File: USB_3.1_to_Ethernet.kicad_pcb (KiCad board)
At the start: 4 copper layers, 76 x 25 mm, 79 parts, among them J1 RJ45_JK0654219, J2 USB3_A, U1 LAN7801_9JX, U2 93LC56B_SN, U3 KSZ9031RNXCC, U4 TLV76733, U5 USBLC6-2P6, U6 TPS7A0212, Y1 25MHz, Y2 25MHz

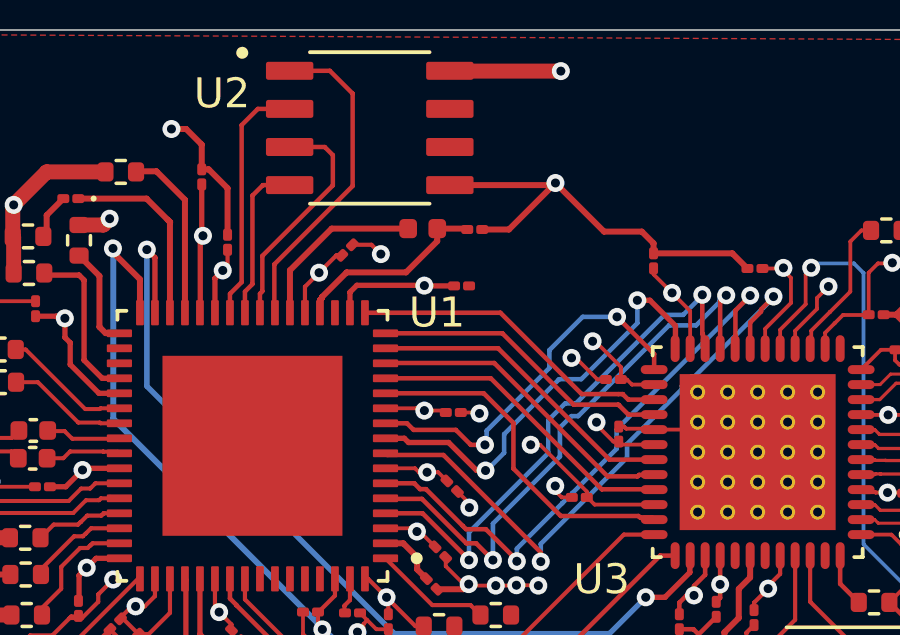
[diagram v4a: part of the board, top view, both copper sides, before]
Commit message: microadjustments  in via connections of  gnd
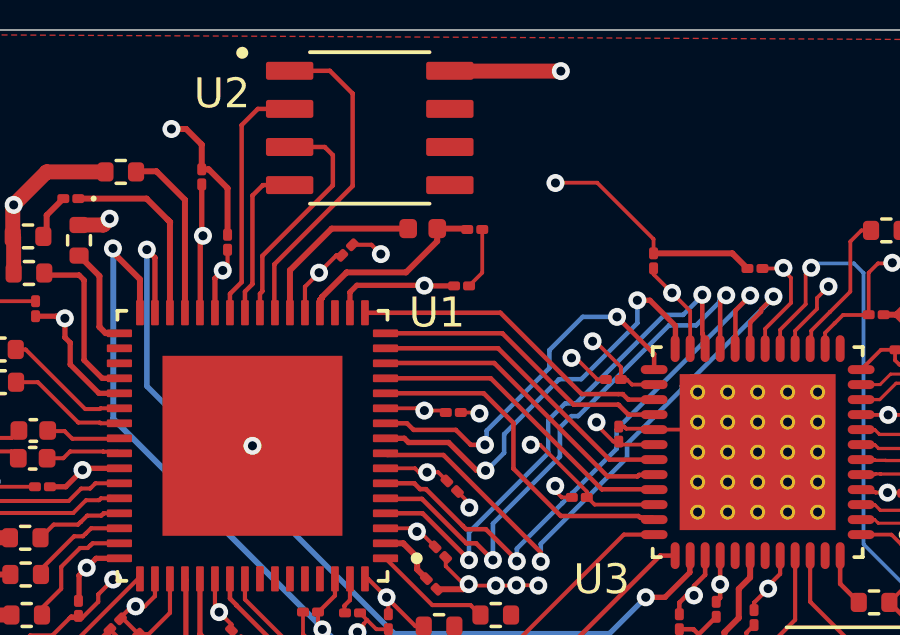
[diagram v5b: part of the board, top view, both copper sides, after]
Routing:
- net GND: track 144.6 -> 140.1 mm, vias 32 -> 33
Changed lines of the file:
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@@
+	)
+	(segment
+		(start 97.67 57.545)
+		(end 97.67 57.07)
+		(width 0.127)
+		(layer "F.Cu")
+		(net "GND")
 	)
 	(segment
@@
 	)
 	(segment
+		(start 94.41 55.19)
+		(end 94.4 55.2)
+		(width 0.127)
+		(layer "F.Cu")
+		(net "GND")
+	)
+	(segment
+		(start 91.96 58.19)
+		(end 91.96 56.75)
+		(width 0.127)
+		(layer "F.Cu")
+		(net "GND")
+	)
+	(segment
 		(start 70.86 72.79)
 		(end 70.52 72.45)
@@
 		(start 76.23 68.25)
 		(end 75.1 68.25)
-		(width 0.2)
-		(layer "F.Cu")
-		(net "GND")
-	)
-	(segment
-		(start 90.88 55.27)
-		(end 94.33 55.27)
 		(width 0.2)
 		(layer "F.Cu")
@@
 	)
 	(segment
+		(start 91.52 58.63)
+		(end 91.96 58.19)
+		(width 0.127)
+		(layer "F.Cu")
+		(net "GND")
+	)
+	(segment
 		(start 83.47 55.373722)
 		(end 83.47 56.925)
-		(width 0.2)
-		(layer "F.Cu")
-		(net "GND")
-	)
-	(segment
-		(start 94.33 55.27)
-		(end 94.4 55.2)
 		(width 0.2)
 		(layer "F.Cu")
@@
 	)
 	(segment
+		(start 97.67 57.07)
+		(end 95.79 55.19)
+		(width 0.127)
+		(layer "F.Cu")
+		(net "GND")
+	)
+	(segment
 		(start 105.26 72.57)
 		(end 106.255 73.565)
@@
 	)
 	(segment
+		(start 95.79 55.19)
+		(end 94.41 55.19)
+		(width 0.127)
+		(layer "F.Cu")
+		(net "GND")
+	)
+	(segment
 		(start 86.396922 70.6427)
 		(end 85.985 70.230778)
@@
 	)
 	(segment
-		(start 97.67 57.21)
-		(end 97.67 57.545)
-		(width 0.2)
-		(layer "F.Cu")
-		(net "GND")
-	)
-	(segment
 		(start 82.61 54.745)
 		(end 82.841278 54.745)
@@
 		(end 97.69 63.42)
 		(width 0.127)
-		(layer "F.Cu")
-		(net "GND")
-	)
-	(segment
-		(start 91.96 56.75)
-		(end 92.85 56.75)
-		(width 0.2)
 		(layer "F.Cu")
 		(net "GND")
@@
 	)
 	(segment
-		(start 96.02 56.82)
-		(end 97.28 56.82)
-		(width 0.2)
-		(layer "F.Cu")
-		(net "GND")
-	)
-	(segment
-		(start 97.28 56.82)
-		(end 97.67 57.21)
-		(width 0.2)
-		(layer "F.Cu")
-		(net "GND")
-	)
-	(segment
 		(start 83.47 73.64)
 		(end 85.25 73.64)
@@
 		(end 94.945001 65.68)
 		(width 0.127)
-		(layer "F.Cu")
-		(net "GND")
-	)
-	(segment
-		(start 94.4 55.2)
-		(end 96.02 56.82)
-		(width 0.2)
 		(layer "F.Cu")
 		(net "GND")
@@
 		(end 96.689658 63.32)
 		(width 0.127)
-		(layer "F.Cu")
-		(net "GND")
-	)
-	(segment
-		(start 92.85 56.75)
-		(end 94.4 55.2)
-		(width 0.2)
 		(layer "F.Cu")
 		(net "GND")
@@
 		(size 0.6)
 		(drill 0.3)
+		(layers "F.Cu" "B.Cu")
+		(net "GND")
+	)
+	(via
+		(at 84.299999 63.96)
+		(size 0.6)
+		(drill 0.3)

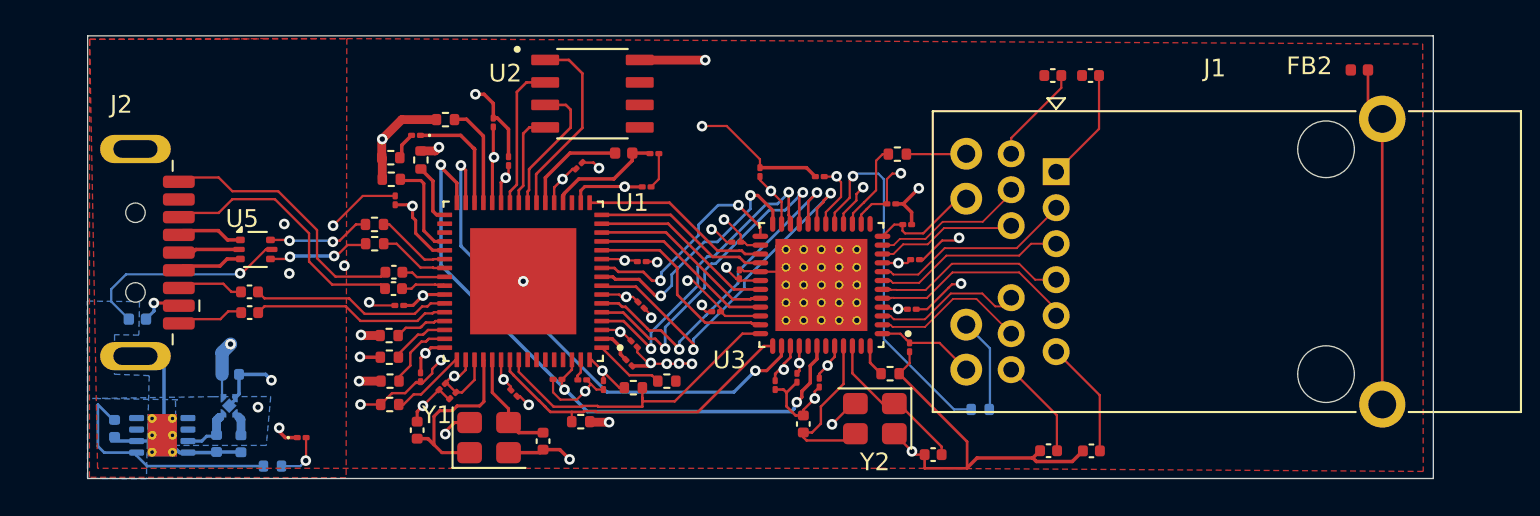
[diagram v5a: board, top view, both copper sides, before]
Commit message: cleaned the DRC errors and step files of ICs included
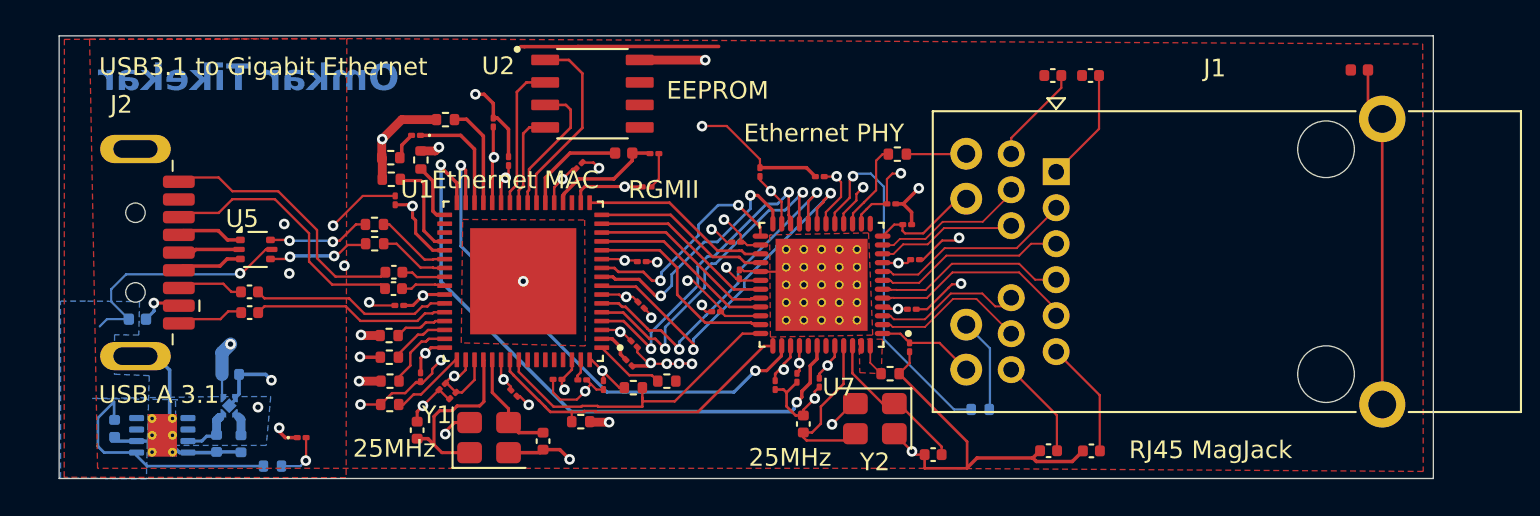
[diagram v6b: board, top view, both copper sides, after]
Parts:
- removed U3: KSZ9031RNXCC, KSZ9031RNX:IC_KSZ9031RNXCC
- added U7: KSZ9031RNXCC, KSZ9031RNXCC:IC_KSZ9031RNXCC, F.Cu at (101.2, 64.2)
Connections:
- C48 pad 1: 3v3_out -> 1v2_core
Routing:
- net GND: track 140.1 -> 151.6 mm
- net 1v2_core: track 125.4 -> 128.4 mm
- net +5V: track 25.6 -> 27.7 mm
- net /~{RESET_N}: track 35.8 -> 36.3 mm
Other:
- board size 76 x 25 mm -> 77.6 x 25 mm
- board text added: "25MHz"
- board text added: "EEPROM"
- board text added: "Ethernet MAC"
- board text added: "Ethernet PHY"
- board text added: "Omkar Tikekar"
- board text added: "RGMII"
- board text added: "RJ45 MagJack"
- board text added: "USB A 3.1"
- board text added: "USB3.1 to Gigabit Ethernet"

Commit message: step file for usb A plug added. Modified edge cuts layer by adding a slot for usb connector'
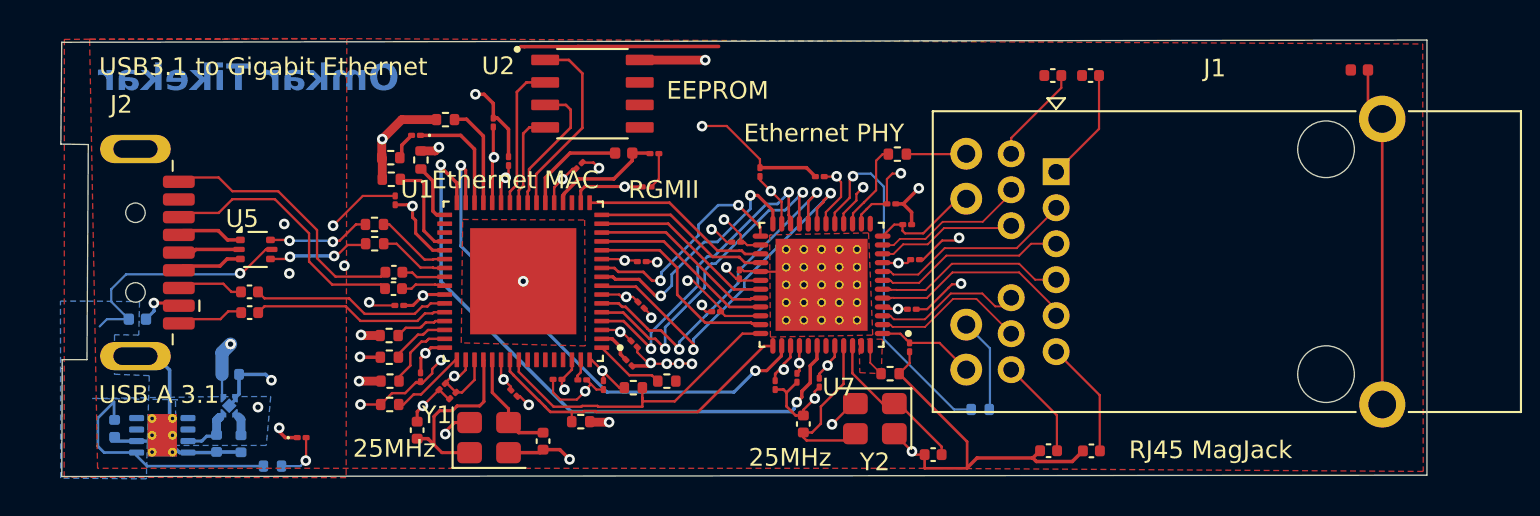
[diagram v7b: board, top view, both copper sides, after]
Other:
- board size 77.6 x 25 mm -> 77.2 x 24.7 mm

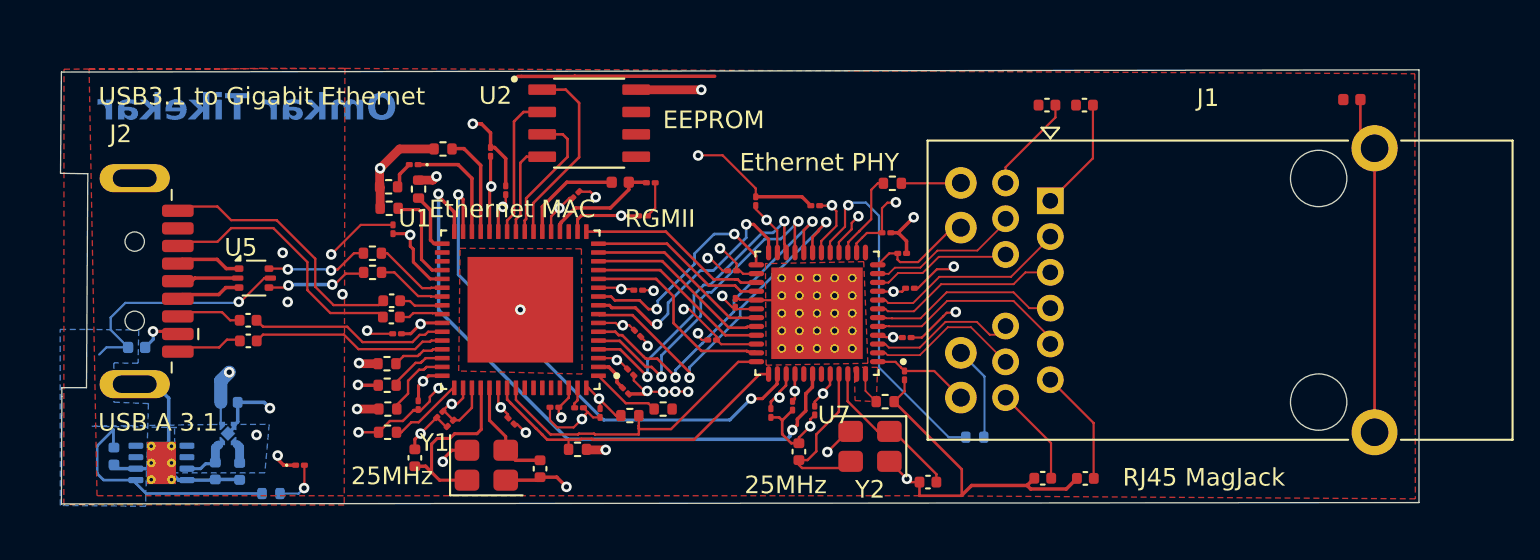
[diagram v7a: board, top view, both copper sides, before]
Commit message: adjusted via positions near the PHY ic
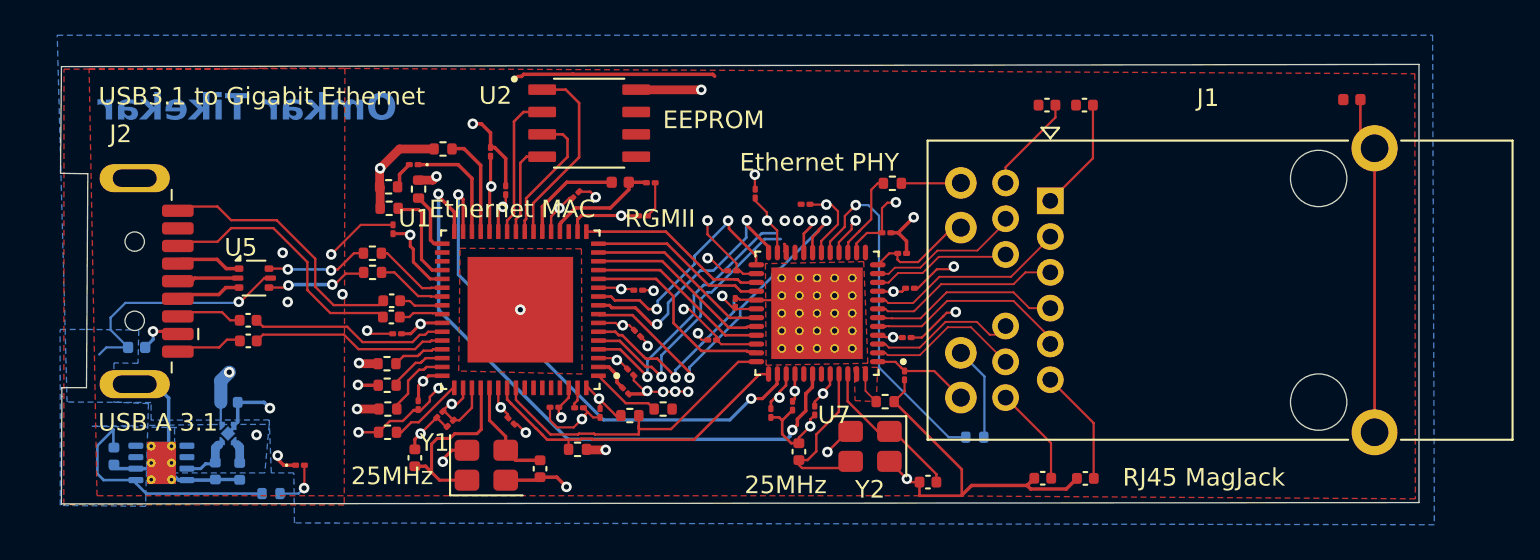
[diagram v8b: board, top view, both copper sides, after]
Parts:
- moved C31 0.56 mm to (100.5, 58.0)
- moved C42 0.43 mm to (97.6, 57.4)
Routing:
- net /TXD1: track 19.5 -> 13.6 mm
- net GND: track 151.6 -> 147.3 mm
- net /TXD2: track 19.1 -> 15.7 mm
- net /TXD3: track 17.9 -> 15.9 mm
- net /TXC: track 12.6 -> 13.5 mm
- net 1v2_core: track 128.4 -> 129.1 mm
- added copper zone on B.Cu, net GND
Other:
- board size 77.2 x 24.7 mm -> 77.2 x 25 mm
